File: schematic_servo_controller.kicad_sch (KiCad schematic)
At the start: 15 parts, among them J1 Conn_01x03, J10 Conn_01x04, J2 Conn_01x03, J3 Conn_01x03, J3 Conn_02x01, J4 Conn_01x03, J5 Conn_01x03, J5 Conn_02x07_Odd_Even, J6 Conn_01x03, J7 Conn_01x03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

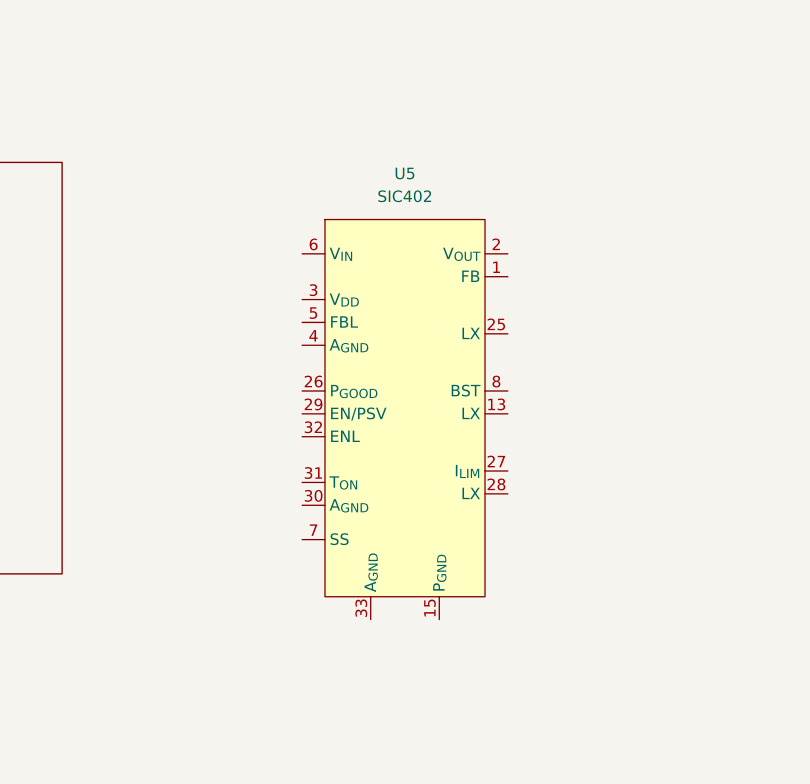
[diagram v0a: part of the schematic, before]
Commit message: change DCDC
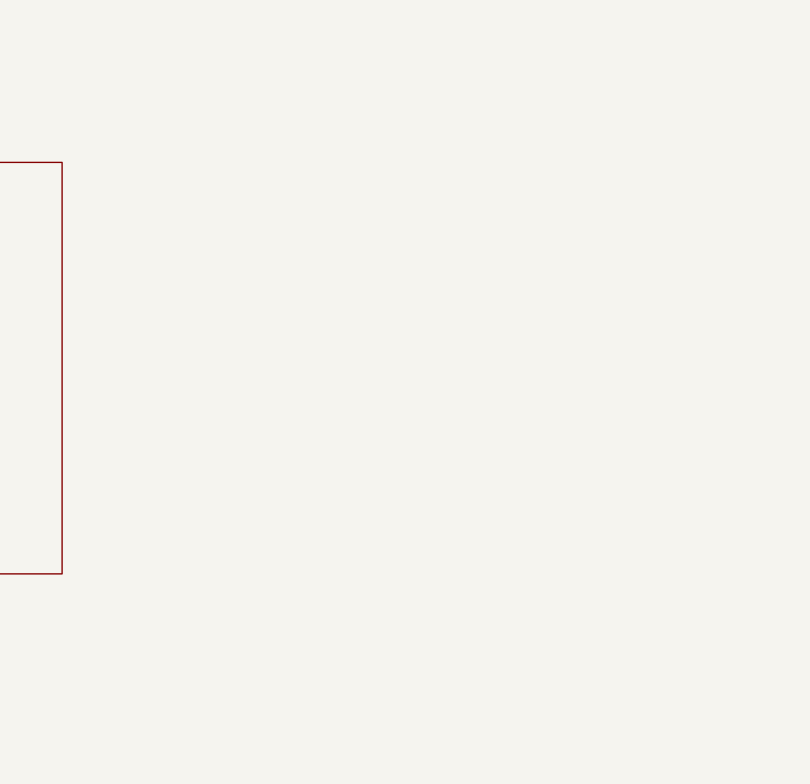
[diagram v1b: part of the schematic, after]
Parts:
- removed U5: SIC402, symbol RDC_generic:SiC402
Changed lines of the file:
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@@
-    )
-  )
-  (symbol (lib_id "RDC_generic:SiC402") (at 189.23 120.65 0) (unit 1)
-    (in_bom yes) (on_board yes) (dnp no) (fields_autoplaced)
-    (property "Reference" "U5" (at 189.23 72.39 0)
-      (effects (font (size 1.27 1.27)))
-    )
-    (property "Value" "SIC402" (at 189.23 74.93 0)
-      (effects (font (size 1.27 1.27)))
-    )
-    (property "Footprint" "" (at 189.23 120.65 0)
-      (effects (font (size 1.27 1.27)) hide)
-    )
-    (property "Datasheet" "" (at 189.23 120.65 0)
-      (effects (font (size 1.27 1.27)) hide)
-    )
-    (pin "13")
-    (pin "11")
-    (pin "2")
-    (pin "26")
-    (pin "27")
-    (pin "17")
-    (pin "3")
-    (pin "1")
-    (pin "31")
-    (pin "35")
-    (pin "4")
-    (pin "22")
-    (pin "32")
-    (pin "9")
-    (pin "14")
-    (pin "20")
-    (pin "12")
-    (pin "25")
-    (pin "28")
-    (pin "29")
-    (pin "19")
-    (pin "33")
-    (pin "7")
-    (pin "21")
-    (pin "23")
-    (pin "24")
-    (pin "34")
-    (pin "30")
-    (pin "6")
-    (pin "8")
-    (pin "5")
-    (pin "15")
-    (pin "16")
-    (pin "18")
-    (pin "10")
-    (instances
-      (project "schematic_servo_controller"
-        (path "/e75aded8-c443-4e1c-9e8d-12c6f0ab47f0"
-          (reference "U5") (unit 1)
-        )
-      )
     )
   )
